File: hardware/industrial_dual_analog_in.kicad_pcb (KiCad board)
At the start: 2 copper layers, 40 x 40 mm, 79 parts, among them P1 CON-SENSOR2, P2 CONN_1, P3 CONN_8, P4 DEBUG, P5 DEBUG, U1 LMV342IDRG4, U2 LM2664, U3 XMC1XXX24, U4 MCP3911, U5 DRILL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

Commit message: Fix routing
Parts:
- removed R26: 82, kicad-libraries:R0603F
- moved P5 1.51 mm to (121.4, 92.8)
- moved R3 1.04 mm to (128.1, 85.5)
- moved R25 0.80 mm to (117.6, 91.1), turned to 180 degrees
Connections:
- RP2 pad 4: Net-(RP2-Pad4) -> M-MOSI
- RP2 pad 5: Net-(RP2-Pad5) -> P0.2
- U3 pad 1: Net-(R26-Pad1) -> P0.2
- U3 pad 2: Net-(P5-Pad2) -> Net-(R25-Pad1)
- U3 pad 7: Net-(R25-Pad1) -> Net-(P5-Pad2)
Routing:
- net Net-(R25-Pad1): track 8.78 -> 3.71 mm, vias 2 -> 0
- net Net-(R26-Pad1): track 3.40 -> 0.00 mm, vias 2 -> 0
- net Net-(P5-Pad2): track 3.42 -> 5.62 mm
- net P0.2: track 0.00 -> 2.08 mm
- net M-MOSI: track 24.2 -> 26.0 mm
- net Net-(D3-Pad2): track 1.42 -> 2.39 mm
- net Net-(R3-Pad2): track 13.9 -> 13.1 mm

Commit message: Add correct logos and replace existing ones
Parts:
- removed the VAL at (142.1, 100.0)
- removed the VAL at (129.1, 100.0)
- added G***: LOGO, kicad-libraries:Logo_CoMCU, B.Cu at (146.1, 116.2)
- added VAL: CE_5mm, kicad-libraries:CE_5mm, B.Cu at (125.1, 116.2)
- added VAL: WEEE_7mm, kicad-libraries:WEEE_7mm, B.Cu at (135.6, 116.2)

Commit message: add status leds
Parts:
- removed R25: 1k, kicad-libraries:R0603F
- added D4: blue, kicad-libraries:D0603F, F.Cu at (148.9, 82.5)
- added D5: blue, kicad-libraries:D0603F, F.Cu at (147.3, 82.5)
- added RP3: 1k, kicad-libraries:4X0402, F.Cu at (126.7, 81.5)
- X1: footprint kicad-libraries:HC49_US -> kicad-libraries:CRYSTAL_3225
- moved D3 29.7 mm to (144.1, 82.5), turned to 270 degrees
- moved P4 6.84 mm to (119.8, 91.3)
- moved RP1 2.71 mm to (126.7, 83.7)
- moved X1 2.39 mm to (144.8, 91.2)
- moved R3 1.50 mm to (129.6, 85.7)
- moved C23 1.25 mm to (126.7, 85.3), turned to 180 degrees
- moved F1 1.00 mm to (150.7, 104.4)
- turned FB1 to 90 degrees
- turned FB2 to 270 degrees
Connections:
- FB1 pad 1: 3V3 -> +3.3VADC
- FB1 pad 2: +3.3VADC -> 3V3
- FB2 pad 1: 3V3 -> +3.3VP
- FB2 pad 2: +3.3VP -> 3V3
- U3 pad 13: Net-(U3-Pad13) -> LED1
- U3 pad 14: Net-(U3-Pad14) -> LED0
- U3 pad 15: Net-(P4-Pad1) -> LEDS
- U3 pad 16: Net-(U3-Pad16) -> (no net)
- U3 pad 17: Net-(U3-Pad17) -> (no net)
- U3 pad 19: Net-(U3-Pad19) -> (no net)
- U3 pad 2: Net-(R25-Pad1) -> Net-(P4-Pad1)
- U3 pad 21: Net-(U3-Pad21) -> (no net)
- U3 pad 3: Net-(U3-Pad3) -> (no net)
- U3 pad 4: Net-(U3-Pad4) -> (no net)
- U3 pad 5: Net-(U3-Pad5) -> (no net)
- U3 pad 6: Net-(U3-Pad6) -> (no net)
- U3 pad 8: Net-(U3-Pad8) -> (no net)
- U4 pad 12: Net-(U4-Pad12) -> (no net)
- U4 pad 13: Net-(U4-Pad13) -> (no net)
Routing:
- net DGND: track 76.3 -> 46.8 mm, vias 19 -> 14
- net Net-(D4-Pad2): track 0.00 -> 24.7 mm, vias 0 -> 2
- net Net-(D5-Pad2): track 0.00 -> 23.6 mm, vias 0 -> 2
- net Net-(D3-Pad2): track 2.39 -> 18.4 mm, vias 0 -> 2
- net 3V3: track 58.0 -> 68.9 mm
- net Net-(C8-Pad2): track 14.7 -> 5.45 mm
- net LEDS: track 0.00 -> 7.83 mm
- net LED0: track 0.00 -> 6.74 mm
- net LED1: track 0.00 -> 5.85 mm
- net Net-(R25-Pad1): track 3.71 -> 0.00 mm
- net Net-(P1-Pad5): track 11.0 -> 8.51 mm
- net Net-(P1-Pad6): track 9.50 -> 7.02 mm
- net +5V: track 29.3 -> 27.2 mm, vias 2 -> 0
- net S-MISO: track 4.40 -> 6.56 mm, vias 0 -> 2
- net S-CS: track 8.07 -> 10.2 mm, vias 0 -> 2
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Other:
- board text added: "0"
- board text added: "1"
- board text added: "S"
- board text removed: "Status"

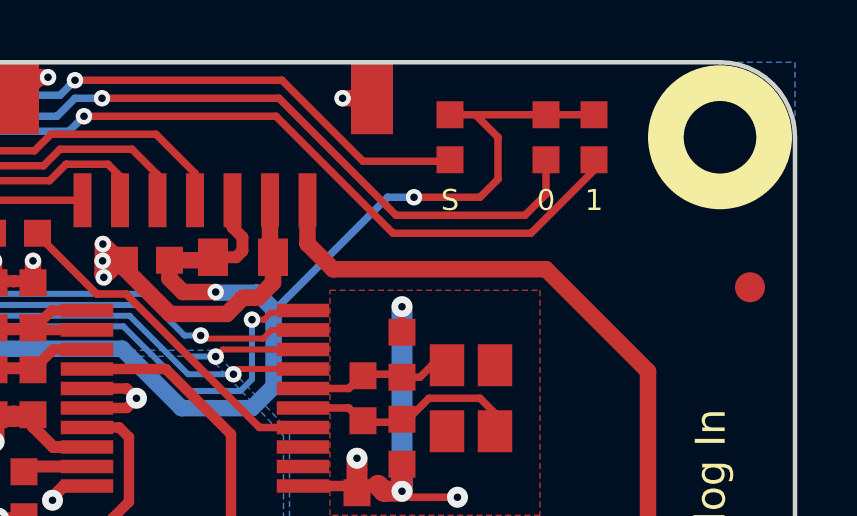
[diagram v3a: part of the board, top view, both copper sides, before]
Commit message: status text fixed
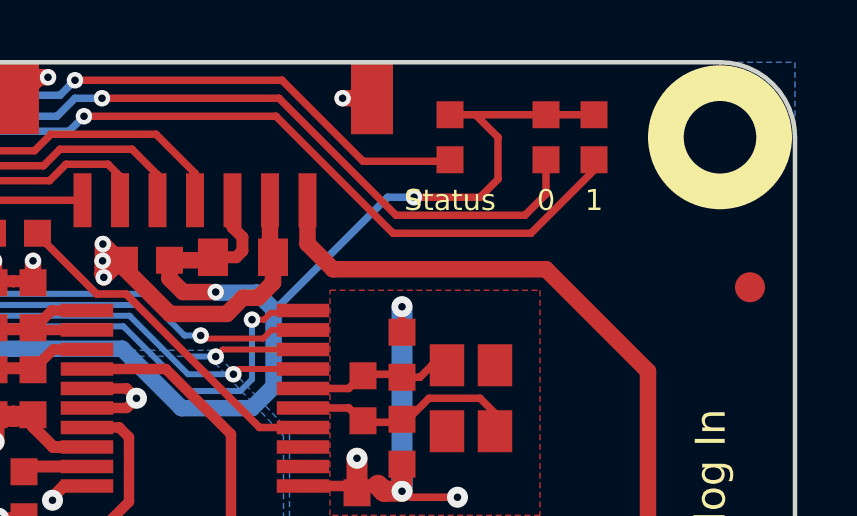
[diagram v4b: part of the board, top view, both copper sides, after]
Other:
- board text added: "Status"
- board text removed: "S"
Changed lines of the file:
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@@
     (links 158)
     (no_connects 1)
-    (area 115.524999 79.924999 155.675001 120.075001)
+    (area 17.19714 79.144999 156.455001 193.31)
     (thickness 1.6)
     (drawings 26)
@@
   (layers
     (0 F.Cu signal)
-    (31 B.Cu signal)
+    (31 B.Cu signal hide)
     (32 B.Adhes user)
     (33 F.Adhes user)
@@
   )
   (setup
-    (last_trace_width 0.7)
+    (last_trace_width 0.254)
     (user_trace_width 0.2)
     (user_trace_width 0.25)
@@
     (effects (font (size 0.7 0.7) (thickness 0.15)))
   )
-  (gr_text S (at 144.1 84.6) (layer F.SilkS)
+  (gr_text Status (at 144.1 84.6) (layer F.SilkS)
     (effects (font (size 0.7 0.7) (thickness 0.15)))
   )
